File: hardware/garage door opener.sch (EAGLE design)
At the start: 26 parts, among them K1 HE3621, K2 HE3621

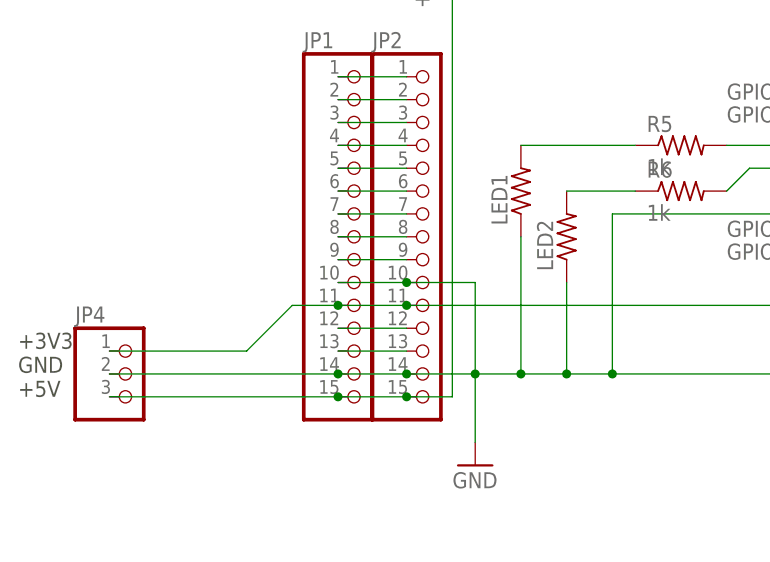
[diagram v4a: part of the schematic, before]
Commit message: removed power header. swapped footprint for led.
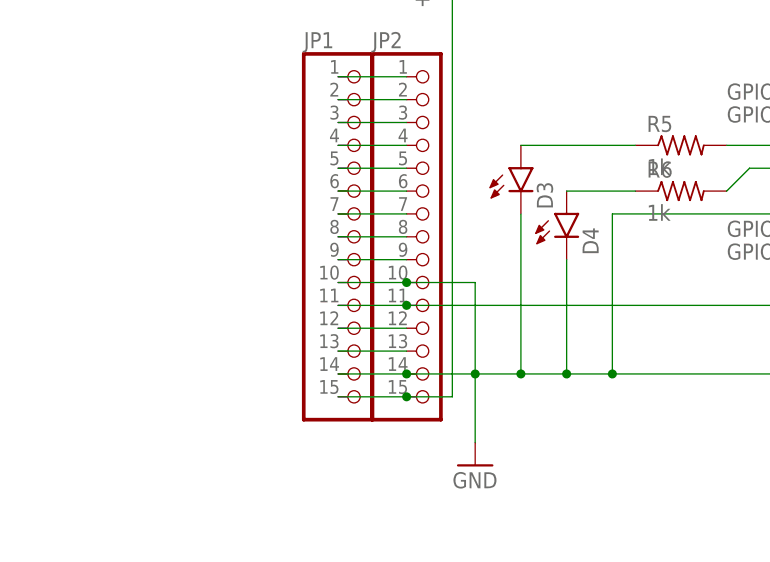
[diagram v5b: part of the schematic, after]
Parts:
- removed JP4: (no value), pinhead:PINHD-1X3
- removed LED1, LED2: (no value), resistor:R-US_R0603
- added D3, D4: (no value), SparkFun-LED:LED0603
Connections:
- net +3V3: no longer JP4.1
- net +5V: no longer JP4.3
- net GND: now also D3.C, D4.C; no longer JP4.2, LED1.1, LED2.1
- net N$28: now also D4.A; no longer LED2.2
- net N$29: now also D3.A; no longer LED1.2
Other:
- note removed: "+3V3 GND +5V"
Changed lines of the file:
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@@
 <layer number="56" name="wert" color="7" fill="1" visible="no" active="no"/>
 <layer number="57" name="tCAD" color="7" fill="1" visible="no" active="no"/>
+<layer number="59" name="tCarbon" color="7" fill="1" visible="no" active="no"/>
+<layer number="60" name="bCarbon" color="7" fill="1" visible="no" active="no"/>
 <layer number="90" name="Modules" color="5" fill="1" visible="yes" active="yes"/>
 <layer number="91" name="Nets" color="2" fill="1" visible="yes" active="yes"/>
@@
 <layer number="127" name="_tValues" color="7" fill="1" visible="no" active="yes"/>
 <layer number="128" name="_bValues" color="7" fill="1" visible="no" active="yes"/>
+<layer number="129" name="Mask" color="7" fill="1" visible="yes" active="yes"/>
 <layer number="131" name="tAdjust" color="7" fill="1" visible="no" active="yes"/>
 <layer number="132" name="bAdjust" color="7" fill="1" visible="no" active="yes"/>
@@
 <layer number="223" name="223bmp" color="24" fill="1" visible="no" active="no"/>
 <layer number="224" name="224bmp" color="25" fill="1" visible="no" active="no"/>
+<layer number="225" name="225bmp" color="7" fill="1" visible="yes" active="yes"/>
+<layer number="226" name="226bmp" color="7" fill="1" visible="yes" active="yes"/>
+<layer number="227" name="227bmp" color="7" fill="1" visible="yes" active="yes"/>
+<layer number="228" name="228bmp" color="7" fill="1" visible="yes" active="yes"/>
+<layer number="229" name="229bmp" color="7" fill="1" visible="yes" active="yes"/>
+<layer number="230" name="230bmp" color="7" fill="1" visible="yes" active="yes"/>
 <layer number="231" name="Eagle3D_PG1" color="7" fill="1" visible="no" active="no"/>
 <layer number="232" name="Eagle3D_PG2" color="7" fill="1" visible="no" active="no"/>
@@
 <layer number="251" name="SMDround" color="7" fill="1" visible="no" active="no"/>
 <layer number="254" name="cooling" color="7" fill="1" visible="no" active="yes"/>
+<layer number="255" name="routoute" color="7" fill="1" visible="yes" active="yes"/>
 </layers>
 <schematic xreflabel="%F%N/%S.%C%R" xrefpart="/%S.%C%R">
@@
 <part name="GND3" library="supply1" deviceset="GND" device=""/>
 <part name="GND4" library="supply1" deviceset="GND" device=""/>
-<part name="LED1" library="resistor" deviceset="R-US_" device="R0603"/>
-<part name="LED2" library="resistor" deviceset="R-US_" device="R0603"/>
 <part name="SENS2" library="adafruit" deviceset="1X2" device="-3.5MM">
 <attribute name="MPN" value="OSTTE020161"/>
@@
 <part name="R4" library="resistor" deviceset="R-US_" device="R0603" value="4k"/>
 <part name="GND5" library="supply1" deviceset="GND" device=""/>
-<part name="JP4" library="pinhead" deviceset="PINHD-1X3" device=""/>
 <part name="R5" library="resistor" deviceset="R-US_" device="R0603" value="1k"/>
 <part name="R6" library="resistor" deviceset="R-US_" device="R0603" value="1k"/>
@@
 <part name="GND6" library="supply1" deviceset="GND" device=""/>
 <part name="GND7" library="supply1" deviceset="GND" device=""/>
+<part name="D3" library="SparkFun-LED" deviceset="LED" device="0603"/>
+<part name="D4" library="SparkFun-LED" deviceset="LED" device="0603"/>
 </parts>
 <sheets>
@@
 <text x="101.6" y="38.1" size="1.778" layer="95">GPIO014</text>
 <text x="101.6" y="35.56" size="1.778" layer="95">GPIO012</text>
-<text x="22.86" y="20.32" size="1.778" layer="97">+3V3
-GND
-+5V</text>
 </plain>
 <instances>
@@
 <instance part="GND3" gate="1" x="48.26" y="73.66"/>
 <instance part="GND4" gate="1" x="55.88" y="73.66"/>
-<instance part="LED1" gate="G$1" x="78.74" y="43.18" rot="R90"/>
-<instance part="LED2" gate="G$1" x="83.82" y="38.1" rot="R90"/>
 <instance part="SENS2" gate="G$1" x="180.34" y="25.4">
 <attribute name="MPN" x="180.34" y="25.4" size="1.778" layer="96" display="off"/>
@@
 <instance part="R4" gate="G$1" x="139.7" y="63.5"/>
 <instance part="GND5" gate="1" x="152.4" y="53.34"/>
-<instance part="JP4" gate="A" x="35.56" y="22.86"/>
 <instance part="R5" gate="G$1" x="96.52" y="48.26"/>
 <instance part="R6" gate="G$1" x="96.52" y="43.18"/>
@@
 <instance part="GND6" gate="1" x="152.4" y="7.62"/>
 <instance part="GND7" gate="1" x="144.78" y="7.62"/>
+<instance part="D3" gate="G$1" x="78.74" y="45.72"/>
+<instance part="D4" gate="G$1" x="83.82" y="40.64"/>
 </instances>
 <busses>
@@
 <wire x1="88.9" y1="40.64" x2="88.9" y2="22.86" width="0.1524" layer="91"/>
 <junction x="88.9" y="22.86"/>
-<pinref part="LED2" gate="G$1" pin="1"/>
-<wire x1="83.82" y1="33.02" x2="83.82" y2="22.86" width="0.1524" layer="91"/>
+<wire x1="83.82" y1="35.56" x2="83.82" y2="22.86" width="0.1524" layer="91"/>
 <junction x="83.82" y="22.86"/>
-<pinref part="LED1" gate="G$1" pin="1"/>
-<wire x1="78.74" y1="38.1" x2="78.74" y2="22.86" width="0.1524" layer="91"/>
+<wire x1="78.74" y1="40.64" x2="78.74" y2="22.86" width="0.1524" layer="91"/>
 <junction x="78.74" y="22.86"/>
-<pinref part="JP4" gate="A" pin="2"/>
-<wire x1="58.42" y1="22.86" x2="33.02" y2="22.86" width="0.1524" layer="91"/>
-<junction x="58.42" y="22.86"/>
+<pinref part="D3" gate="G$1" pin="C"/>
+<pinref part="D4" gate="G$1" pin="C"/>
 </segment>
 <segment>
@@
 <junction x="66.04" y="30.48"/>
 <junction x="111.76" y="30.48"/>
-<wire x1="58.42" y1="30.48" x2="53.34" y2="30.48" width="0.1524" layer="91"/>
-<junction x="58.42" y="30.48"/>
-<pinref part="JP4" gate="A" pin="1"/>
-<wire x1="53.34" y1="30.48" x2="48.26" y2="25.4" width="0.1524" layer="91"/>
-<wire x1="48.26" y1="25.4" x2="33.02" y2="25.4" width="0.1524" layer="91"/>
 </segment>
 <segment>
@@
 <wire x1="71.12" y1="20.32" x2="66.04" y2="20.32" width="0.1524" layer="91"/>
 <junction x="66.04" y="20.32"/>
-<pinref part="JP4" gate="A" pin="3"/>
-<wire x1="58.42" y1="20.32" x2="33.02" y2="20.32" width="0.1524" layer="91"/>
-<junction x="58.42" y="20.32"/>
 </segment>
 <segment>
@@
 <segment>
 <pinref part="R6" gate="G$1" pin="1"/>
-<pinref part="LED2" gate="G$1" pin="2"/>
 <wire x1="91.44" y1="43.18" x2="83.82" y2="43.18" width="0.1524" layer="91"/>
+<pinref part="D4" gate="G$1" pin="A"/>
 </segment>
 </net>
@@
 <segment>
 <pinref part="R5" gate="G$1" pin="1"/>
-<pinref part="LED1" gate="G$1" pin="2"/>
 <wire x1="91.44" y1="48.26" x2="78.74" y2="48.26" width="0.1524" layer="91"/>
+<pinref part="D3" gate="G$1" pin="A"/>
 </segment>
 </net>
@@
 </schematic>
 </drawing>
-<compatibility>
-<note version="6.3" minversion="6.2.2" severity="warning">
-Since Version 6.2.2 text objects can contain more than one line,
-which will not be processed correctly with this version.
-</note>
-</compatibility>
 </eagle>

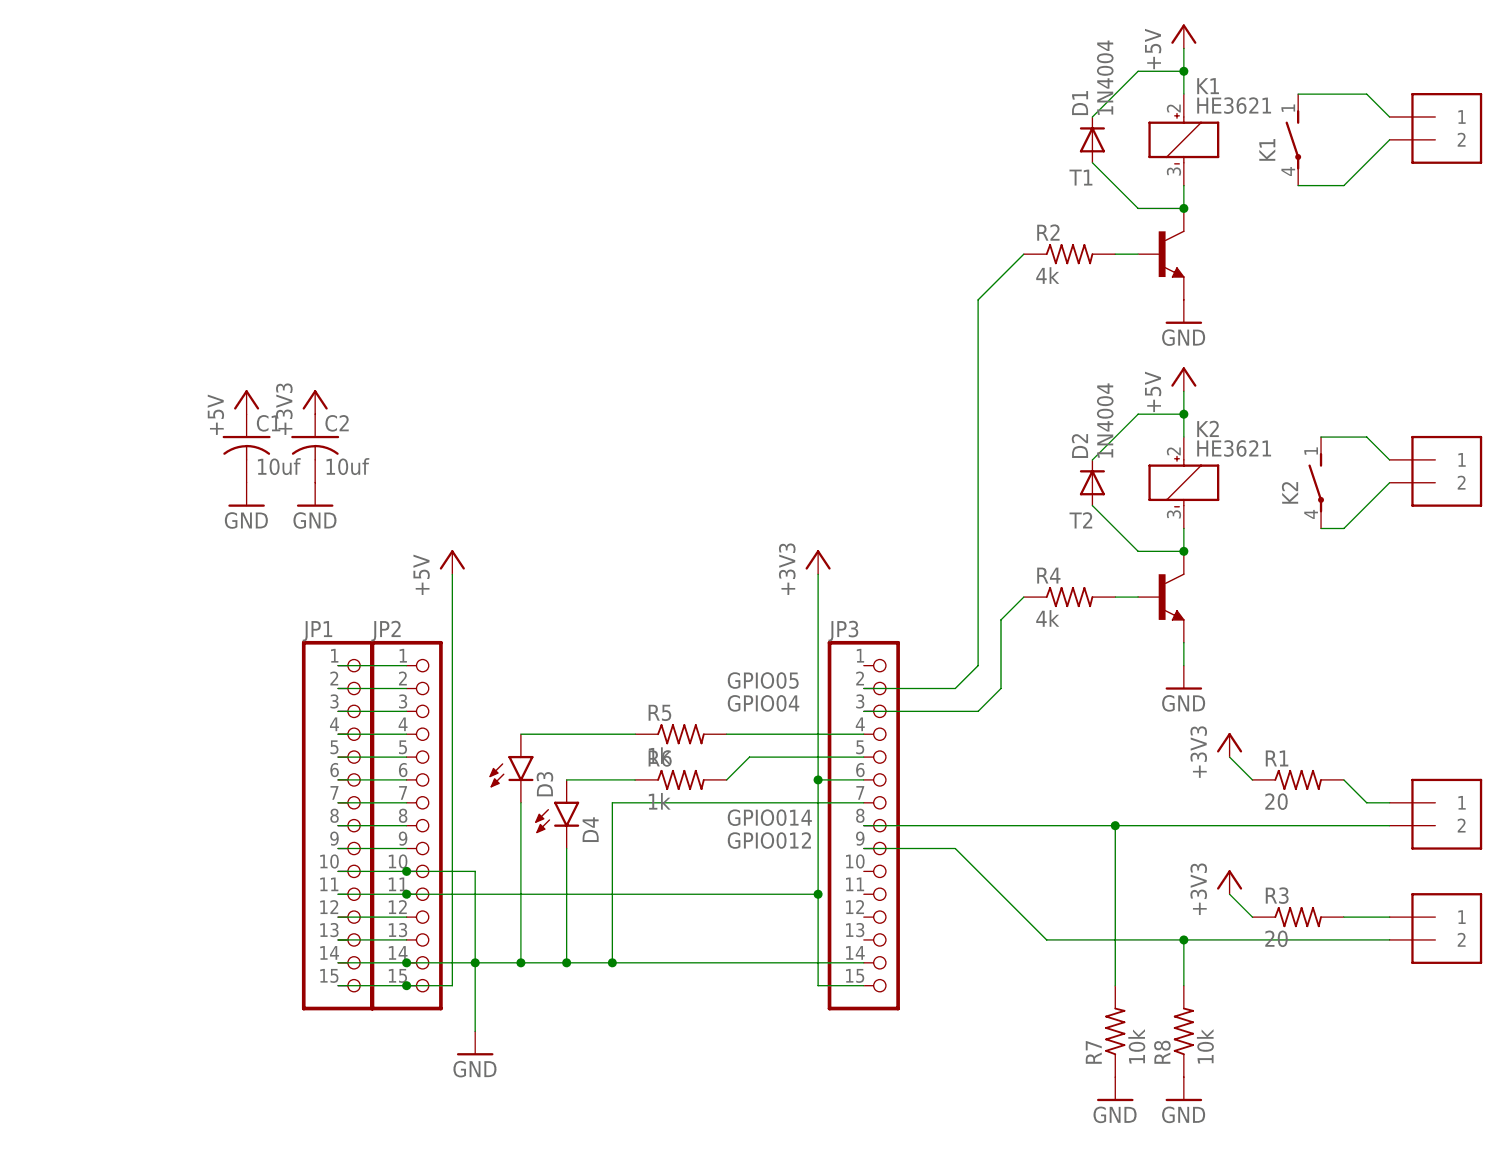
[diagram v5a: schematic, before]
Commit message: Updated with footprint for ds18b20 ... why? feature creep!
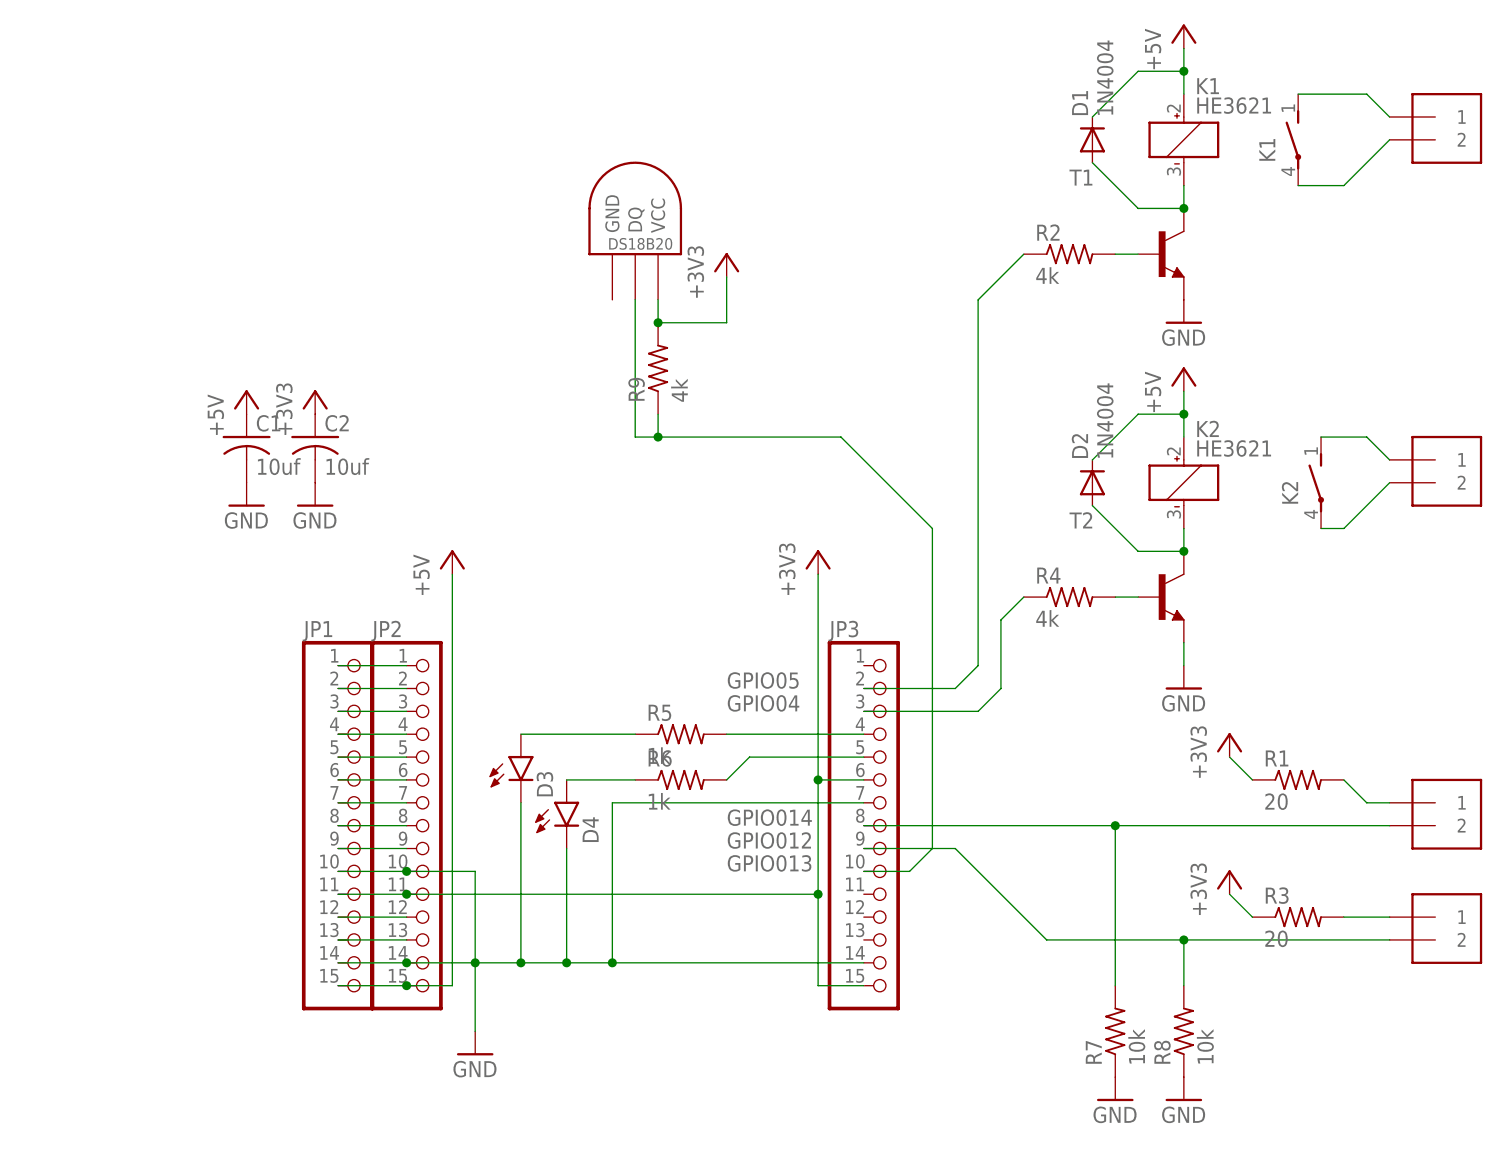
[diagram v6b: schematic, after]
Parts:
- added DS18B20: DS18B20TO92, Ava:DS1820TO92
- added R9: 4k, resistor:R-US_R0603
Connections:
- new net N$30: DS18B20.DQ, JP3.10, R9.1
- net +3V3: now also DS18B20.VCC, R9.2
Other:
- note added: "GPIO013"
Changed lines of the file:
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@@
 <part name="D3" library="SparkFun-LED" deviceset="LED" device="0603"/>
 <part name="D4" library="SparkFun-LED" deviceset="LED" device="0603"/>
+<part name="DS18B20" library="Ava" deviceset="DS1820" device="TO92" value="DS18B20TO92"/>
+<part name="+3V5" library="supply1" deviceset="+3V3" device=""/>
+<part name="R9" library="resistor" deviceset="R-US_" device="R0603" value="4k"/>
 </parts>
 <sheets>
@@
 <text x="101.6" y="38.1" size="1.778" layer="95">GPIO014</text>
 <text x="101.6" y="35.56" size="1.778" layer="95">GPIO012</text>
+<text x="101.6" y="33.02" size="1.778" layer="95">GPIO013</text>
 </plain>
 <instances>
@@
 <instance part="D3" gate="G$1" x="78.74" y="45.72"/>
 <instance part="D4" gate="G$1" x="83.82" y="40.64"/>
+<instance part="DS18B20" gate="G$1" x="91.44" y="101.6"/>
+<instance part="+3V5" gate="G$1" x="101.6" y="101.6"/>
+<instance part="R9" gate="G$1" x="93.98" y="88.9" rot="R90"/>
 </instances>
 <busses>
@@
 <wire x1="160.02" y1="27.94" x2="157.48" y2="30.48" width="0.1524" layer="91"/>
 </segment>
+<segment>
+<pinref part="DS18B20" gate="G$1" pin="VCC"/>
+<wire x1="93.98" y1="96.52" x2="93.98" y2="93.98" width="0.1524" layer="91"/>
+<wire x1="93.98" y1="93.98" x2="101.6" y2="93.98" width="0.1524" layer="91"/>
+<pinref part="+3V5" gate="G$1" pin="+3V3"/>
+<wire x1="101.6" y1="93.98" x2="101.6" y2="99.06" width="0.1524" layer="91"/>
+<pinref part="R9" gate="G$1" pin="2"/>
+<junction x="93.98" y="93.98"/>
+</segment>
 </net>
 <net name="+5V" class="0">
@@
 </segment>
 </net>
+<net name="N$30" class="0">
+<segment>
+<pinref part="DS18B20" gate="G$1" pin="DQ"/>
+<wire x1="91.44" y1="96.52" x2="91.44" y2="81.28" width="0.1524" layer="91"/>
+<wire x1="91.44" y1="81.28" x2="93.98" y2="81.28" width="0.1524" layer="91"/>
+<pinref part="R9" gate="G$1" pin="1"/>
+<wire x1="93.98" y1="81.28" x2="93.98" y2="83.82" width="0.1524" layer="91"/>
+<pinref part="JP3" gate="A" pin="10"/>
+<wire x1="116.84" y1="33.02" x2="121.92" y2="33.02" width="0.1524" layer="91"/>
+<wire x1="121.92" y1="33.02" x2="124.46" y2="35.56" width="0.1524" layer="91"/>
+<wire x1="124.46" y1="35.56" x2="124.46" y2="71.12" width="0.1524" layer="91"/>
+<wire x1="124.46" y1="71.12" x2="114.3" y2="81.28" width="0.1524" layer="91"/>
+<wire x1="114.3" y1="81.28" x2="93.98" y2="81.28" width="0.1524" layer="91"/>
+<junction x="93.98" y="81.28"/>
+</segment>
+</net>
